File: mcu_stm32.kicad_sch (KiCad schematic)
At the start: 20 parts, among them J1 Debug, J2 Boot_Sel, SW1 RESET, U1 STM32F103C8Tx, Y1 8mHz

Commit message: esp32 silindi, yerleştirmeler yapıldı
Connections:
- net SWCLK: now also J1.3; no longer J1.2
- net SWDIO: now also J1.2; no longer J1.3
- net USB_D+: no longer names the net of U1.33 (PA12)
- net USB_D-: no longer names the net of U1.32 (PA11)
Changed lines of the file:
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@@
-		)
-	)
-	(global_label "USB_D+"
-		(shape input)
-		(at 58.42 55.88 0)
-		(fields_autoplaced yes)
-		(effects
-			(font
-				(size 1.27 1.27)
-			)
-			(justify left)
-		)
-		(property "Intersheetrefs" "${INTERSHEET_REFS}"
-			(at 69.0252 55.88 0)
-			(effects
-				(font
-					(size 1.27 1.27)
-				)
-				(justify left)
-				(hide yes)
-			)
 		)
 	)
@@
 	(global_label "SWCLK"
 		(shape input)
+		(at 147.32 82.55 0)
+		(fields_autoplaced yes)
+		(effects
+			(font
+				(size 1.27 1.27)
+			)
+			(justify left)
+		)
+		(property "Intersheetrefs" "${INTERSHEET_REFS}"
+			(at 156.5342 82.55 0)
+			(effects
+				(font
+					(size 1.27 1.27)
+				)
+				(justify left)
+				(hide yes)
+			)
+		)
+	)
+	(global_label "OSC_IN"
+		(shape input)
+		(at 25.4 35.56 180)
+		(fields_autoplaced yes)
+		(effects
+			(font
+				(size 1.27 1.27)
+			)
+			(justify right)
+		)
+		(property "Intersheetrefs" "${INTERSHEET_REFS}"
+			(at 15.7019 35.56 0)
+			(effects
+				(font
+					(size 1.27 1.27)
+				)
+				(justify right)
+				(hide yes)
+			)
+		)
+	)
+	(global_label "3V3"
+		(shape input)
+		(at 116.84 41.91 180)
+		(fields_autoplaced yes)
+		(effects
+			(font
+				(size 1.27 1.27)
+			)
+			(justify right)
+		)
+		(property "Intersheetrefs" "${INTERSHEET_REFS}"
+			(at 110.3472 41.91 0)
+			(effects
+				(font
+					(size 1.27 1.27)
+				)
+				(justify right)
+				(hide yes)
+			)
+		)
+	)
+	(global_label "3V3"
+		(shape input)
+		(at 124.46 78.74 90)
+		(fields_autoplaced yes)
+		(effects
+			(font
+				(size 1.27 1.27)
+			)
+			(justify left)
+		)
+		(property "Intersheetrefs" "${INTERSHEET_REFS}"
+			(at 124.46 72.2472 90)
+			(effects
+				(font
+					(size 1.27 1.27)
+				)
+				(justify left)
+				(hide yes)
+			)
+		)
+	)
+	(global_label "SWDIO"
+		(shape input)
 		(at 147.32 85.09 0)
 		(fields_autoplaced yes)
@@
 		)
 		(property "Intersheetrefs" "${INTERSHEET_REFS}"
-			(at 156.5342 85.09 0)
-			(effects
-				(font
-					(size 1.27 1.27)
-				)
-				(justify left)
-				(hide yes)
-			)
-		)
-	)
-	(global_label "OSC_IN"
-		(shape input)
-		(at 25.4 35.56 180)
-		(fields_autoplaced yes)
-		(effects
-			(font
-				(size 1.27 1.27)
-			)
-			(justify right)
-		)
-		(property "Intersheetrefs" "${INTERSHEET_REFS}"
-			(at 15.7019 35.56 0)
-			(effects
-				(font
-					(size 1.27 1.27)
-				)
-				(justify right)
-				(hide yes)
-			)
-		)
-	)
-	(global_label "3V3"
-		(shape input)
-		(at 116.84 41.91 180)
-		(fields_autoplaced yes)
-		(effects
-			(font
-				(size 1.27 1.27)
-			)
-			(justify right)
-		)
-		(property "Intersheetrefs" "${INTERSHEET_REFS}"
-			(at 110.3472 41.91 0)
-			(effects
-				(font
-					(size 1.27 1.27)
-				)
-				(justify right)
-				(hide yes)
-			)
-		)
-	)
-	(global_label "USB_D-"
-		(shape input)
-		(at 58.42 53.34 0)
-		(fields_autoplaced yes)
-		(effects
-			(font
-				(size 1.27 1.27)
-			)
-			(justify left)
-		)
-		(property "Intersheetrefs" "${INTERSHEET_REFS}"
-			(at 69.0252 53.34 0)
-			(effects
-				(font
-					(size 1.27 1.27)
-				)
-				(justify left)
-				(hide yes)
-			)
-		)
-	)
-	(global_label "3V3"
-		(shape input)
-		(at 124.46 78.74 90)
-		(fields_autoplaced yes)
-		(effects
-			(font
-				(size 1.27 1.27)
-			)
-			(justify left)
-		)
-		(property "Intersheetrefs" "${INTERSHEET_REFS}"
-			(at 124.46 72.2472 90)
-			(effects
-				(font
-					(size 1.27 1.27)
-				)
-				(justify left)
-				(hide yes)
-			)
-		)
-	)
-	(global_label "SWDIO"
-		(shape input)
-		(at 147.32 82.55 0)
-		(fields_autoplaced yes)
-		(effects
-			(font
-				(size 1.27 1.27)
-			)
-			(justify left)
-		)
-		(property "Intersheetrefs" "${INTERSHEET_REFS}"
-			(at 156.1714 82.55 0)
-			(effects
-				(font
+			(at 156.1714 85.09 0)
+			(effects
+				(font

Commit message: Routing
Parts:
- removed J2: Boot_Sel, Connector_PinHeader_2.54mm:PinHeader_2x03_P2.54mm_Vertical, symbol PCM_SL_Pin_Headers:PINHD_2x3_Male
- removed R6, R7: 100K, Resistor_SMD:R_0805_2012Metric, symbol Device:R_Small
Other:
- note removed: "Boot Selection Headers"

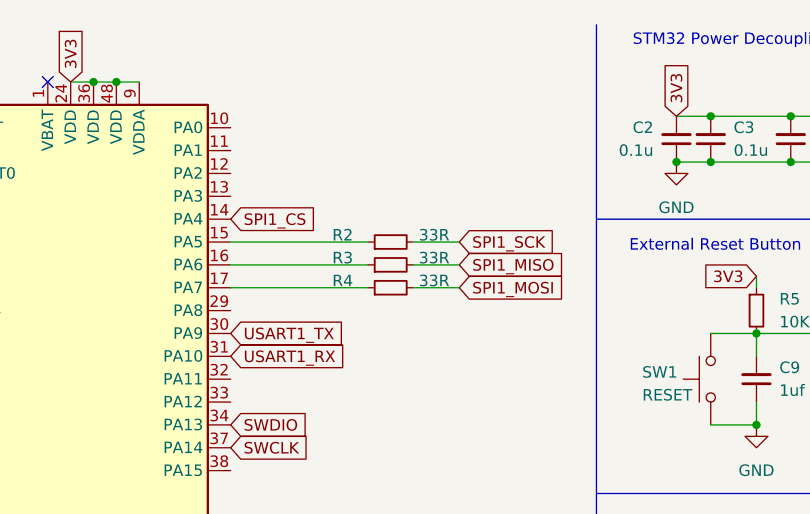
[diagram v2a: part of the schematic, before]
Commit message: yerleştirme tamamlandı
3d modeller eklenecek
drc kontrolü yapılacak
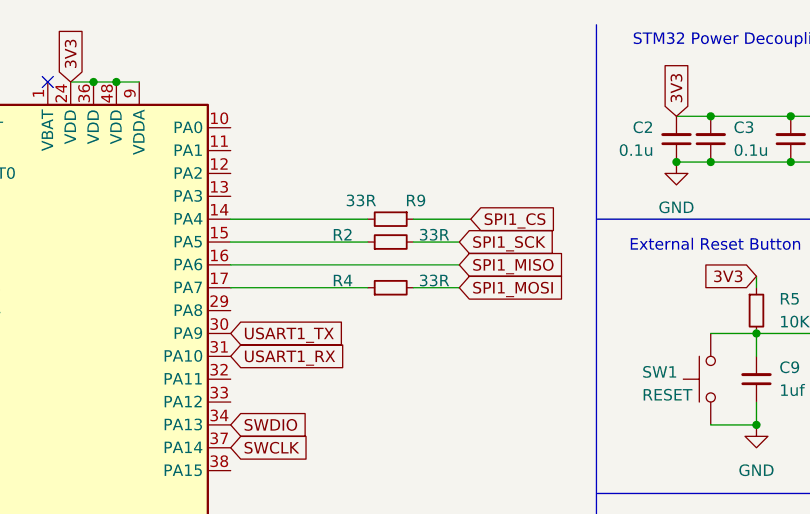
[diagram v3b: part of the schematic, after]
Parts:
- removed R3: 33R, Resistor_SMD:R_0805_2012Metric, symbol Device:R_Small
- added R9: 33R, Resistor_SMD:R_0805_2012Metric, symbol Device:R_Small
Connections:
- net SPI1_CS: now also R9.1; no longer U1.14 (PA4)
- net SPI1_MISO: now also U1.16 (PA6)
- new net: R9.2, U1.14 (PA4)
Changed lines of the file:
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@@
 	(wire
 		(pts
-			(xy 73.66 40.64) (xy 58.42 40.64)
+			(xy 58.42 40.64) (xy 83.82 40.64)
 		)
 		(stroke
@@
 		)
 	)
+	(wire
+		(pts
+			(xy 85.09 35.56) (xy 78.74 35.56)
+		)
+		(stroke
+			(width 0)
+			(type default)
+		)
+	)
 	(polyline
 		(pts
@@
 	(wire
 		(pts
-			(xy 147.32 80.01) (xy 158.75 80.01)
+			(xy 73.66 35.56) (xy 58.42 35.56)
 		)
 		(stroke
@@
 	(wire
 		(pts
-			(xy 111.76 58.42) (xy 116.84 58.42)
+			(xy 147.32 80.01) (xy 158.75 80.01)
 		)
 		(stroke
@@
 	(wire
 		(pts
-			(xy 83.82 40.64) (xy 78.74 40.64)
+			(xy 111.76 58.42) (xy 116.84 58.42)
 		)
 		(stroke
@@
 	(global_label "SPI1_CS"
 		(shape input)
-		(at 58.42 35.56 0)
+		(at 85.09 35.56 0)
 		(fields_autoplaced yes)
 		(effects
@@
 		)
 		(property "Intersheetrefs" "${INTERSHEET_REFS}"
-			(at 69.1461 35.56 0)
+			(at 95.8161 35.56 0)
 			(effects
 				(font
@@
 	)
 	(symbol
-		(lib_id "Device:R_Small")
-		(at 76.2 40.64 90)
-		(unit 1)
-		(exclude_from_sim no)
-		(in_bom yes)
-		(on_board yes)
-		(dnp no)
-		(property "Reference" "R3"
-			(at 70.866 39.878 90)
-			(effects
-				(font
-					(size 1.27 1.27)
-				)
-			)
-		)
-		(property "Value" "33R"
-			(at 81.026 39.878 90)
-			(effects
-				(font
-					(size 1.27 1.27)
-				)
-			)
-		)
-		(property "Footprint" "Resistor_SMD:R_0805_2012Metric"
-			(at 76.2 40.64 0)
-			(effects
-				(font
-					(size 1.27 1.27)
-				)
-				(hide yes)
-			)
-		)
-		(property "Datasheet" "~"
-			(at 76.2 40.64 0)
-			(effects
-				(font
-					(size 1.27 1.27)
-				)
-				(hide yes)
-			)
-		)
-		(property "Description" "Resistor, small symbol"
-			(at 76.2 40.64 0)
-			(effects
-				(font
-					(size 1.27 1.27)
-				)
-				(hide yes)
-			)
-		)
-		(pin "1"
-		)
-		(pin "2"
-		)
-		(instances
-			(project "controllerForVehicle"
-				(path "/f177fb06-71dc-4865-9331-a828b12c2bf7/3df2cc68-9e37-4ed2-a8f2-6c459eac7ab6"
-					(reference "R3")
-					(unit 1)
-				)
-			)
-		)
-	)
-	(symbol
 		(lib_id "power:GND")
 		(at 147.32 27.94 270)
@@
 					(unit 1)
 				)
+			)
+		)
+	)
+	(symbol
+		(lib_id "Device:R_Small")
+		(at 76.2 35.56 270)
+		(unit 1)
+		(exclude_from_sim no)
+		(in_bom yes)
+		(on_board yes)
+		(dnp no)
+		(property "Reference" "R9"
+			(at 78.994 33.528 90)
+			(effects
+				(font
+					(size 1.27 1.27)
+				)
+			)
+		)
+		(property "Value" "33R"
+			(at 72.898 33.528 90)
+			(effects
+				(font
+					(size 1.27 1.27)
+				)
+			)
+		)
+		(property "Footprint" "Resistor_SMD:R_0805_2012Metric"
+			(at 76.2 35.56 0)
+			(effects
+				(font
+					(size 1.27 1.27)
+				)
+				(hide yes)
+			)
+		)
+		(property "Datasheet" "~"
+			(at 76.2 35.56 0)
+			(effects
+				(font
+					(size 1.27 1.27)
+				)
+				(hide yes)
+			)
+		)
+		(property "Description" "Resistor, small symbol"
+			(at 76.2 35.56 0)
+			(effects
+				(font
+					(size 1.27 1.27)
+				)
+				(hide yes)
+			)
+		)
+		(pin "1"
+		)
+		(pin "2"
+		)
+		(instances
+			(project "controllerForVehicle"
+				(path "/f177fb06-71dc-4865-9331-a828b12c2bf7/3df2cc68-9e37-4ed2-a8f2-6c459eac7ab6"
+					(reference "R9")
+					(unit 1)
+				)
